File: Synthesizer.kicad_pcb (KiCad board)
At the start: 6 copper layers, 167 parts, among them J1 USB_A, J2 AudioJack3, J3 USB_B_Micro, J4 FPGA_debug, J5 MCU_debug, J6 67997-410HLF, SW1 SW_Push, SW10 SW_Push, SW11 SW_Push, SW12 SW_Push, SW13 SW_Push, SW14 SW_Push, SW15 SW_Push, SW16 SW_Push, SW2 SW_Push, SW3 SW_Push, SW4 SW_Push, SW5 SW_Push, SW6 SW_Push, SW7 SW_Push, SW8 SW_Push, SW9 SW_Push, U1 TPD3S014, U2 S25FL127S, U3 XC7A100T-FTG256, U4 Oscillator, U5 TPS54325, U6 TPS54294, U7 EFM32GG11B4xx, U8 PCM5102, Y1 48Mhz

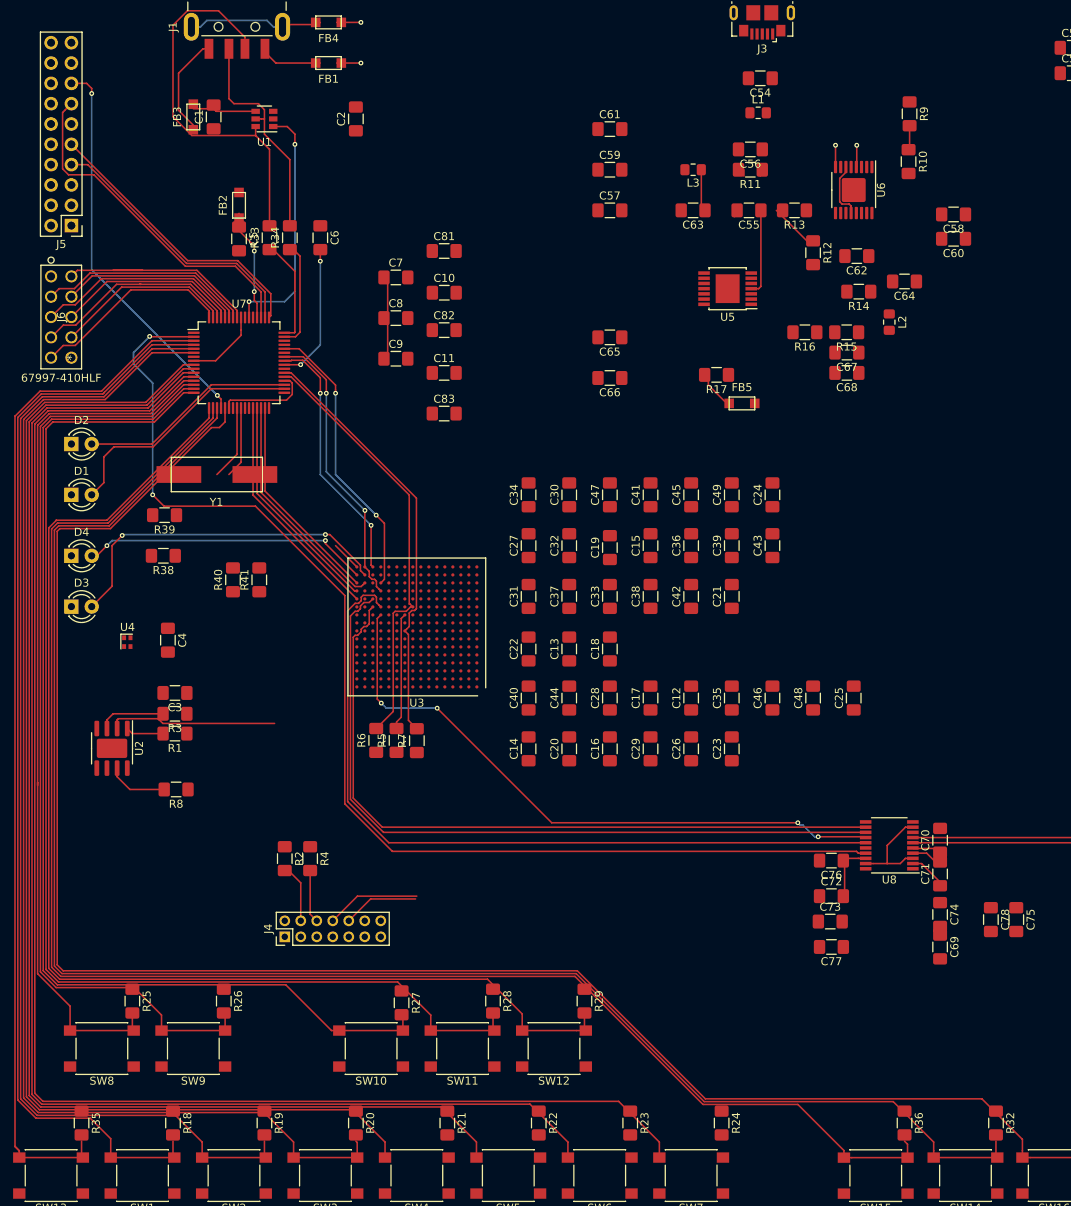
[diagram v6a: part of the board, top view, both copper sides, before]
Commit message: Added in the potentiometers, fixed some faulty pins on the artix, rewired some pins on the MCU so they didn't interfere with the crystal.
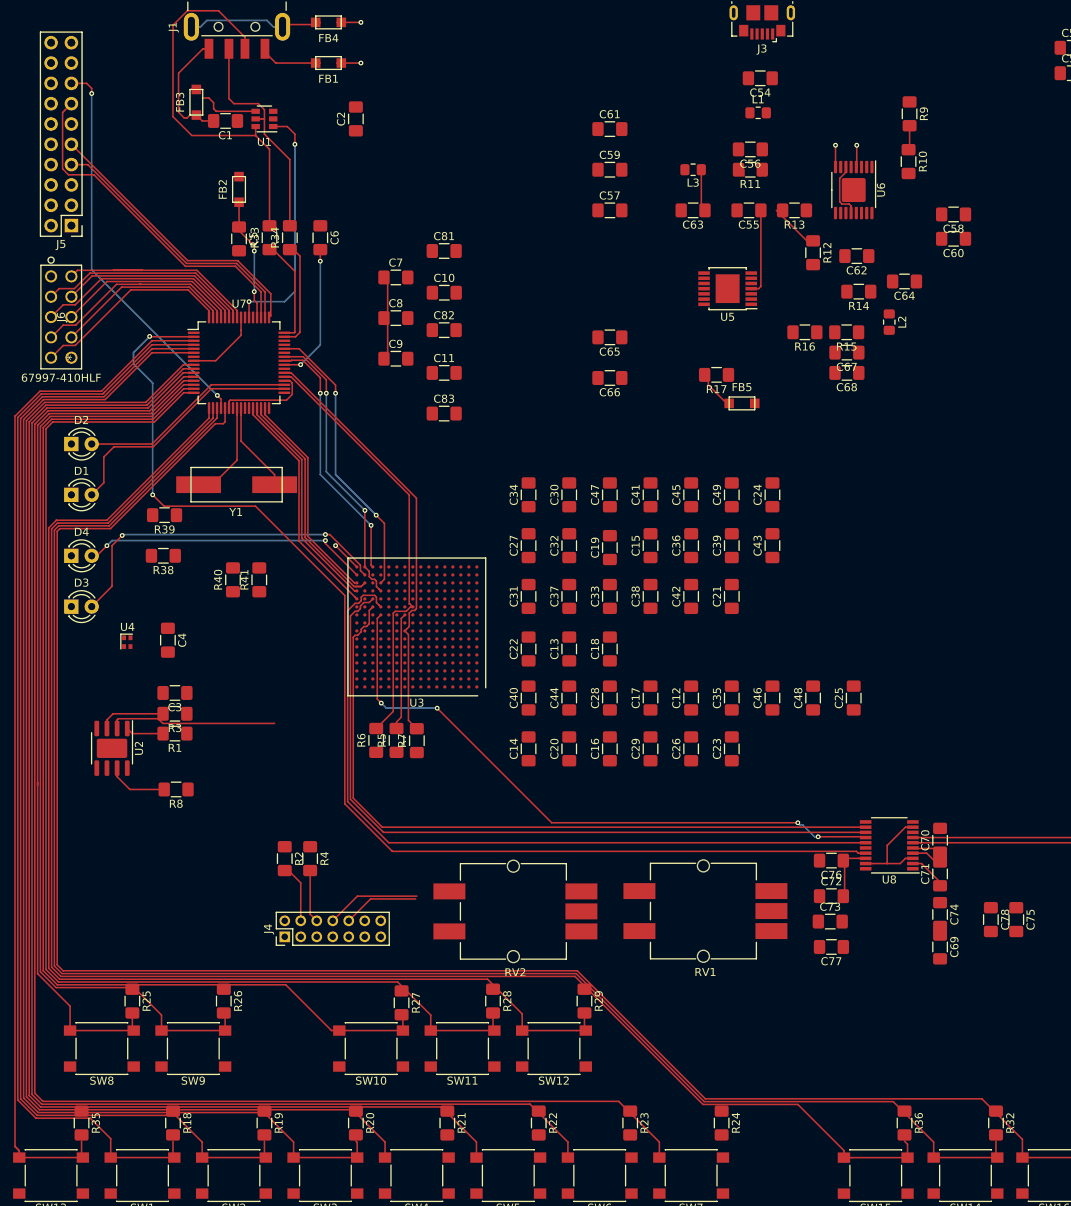
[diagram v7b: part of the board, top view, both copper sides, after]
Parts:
- added RV1: R_POT, Potentiometer_SMD:Potentiometer_Bourns_PRS11S_Vertical, F.Cu at (99.6, 125.7)
- added RV2: R_POT, Potentiometer_SMD:Potentiometer_Bourns_PRS11S_Vertical, F.Cu at (75.8, 125.7)
- moved Y1 2.77 mm to (41.0, 72.4)
- moved FB2 1.98 mm to (41.3, 35.5)
- moved FB3 1.88 mm to (35.9, 24.6)
- moved C1 1.57 mm to (39.6, 26.9), turned to 180 degrees
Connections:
- U7 pad 36: GND -> Net-(U7-Pad36)
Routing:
- net Net-(FB3-Pad1): track 0.00 -> 7.78 mm
- net Net-(C1-Pad2): track 20.2 -> 15.1 mm
- net Net-(U7-Pad24): track 9.35 -> 12.6 mm
- net Net-(U7-Pad25): track 8.94 -> 11.3 mm
- net /Artix7/SPI_CLK: track 28.6 -> 29.4 mm
- net Net-(C5-Pad1): track 14.3 -> 14.9 mm
- net GND: vias 6 -> 7
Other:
- board text added: "5V might need thicker trace"

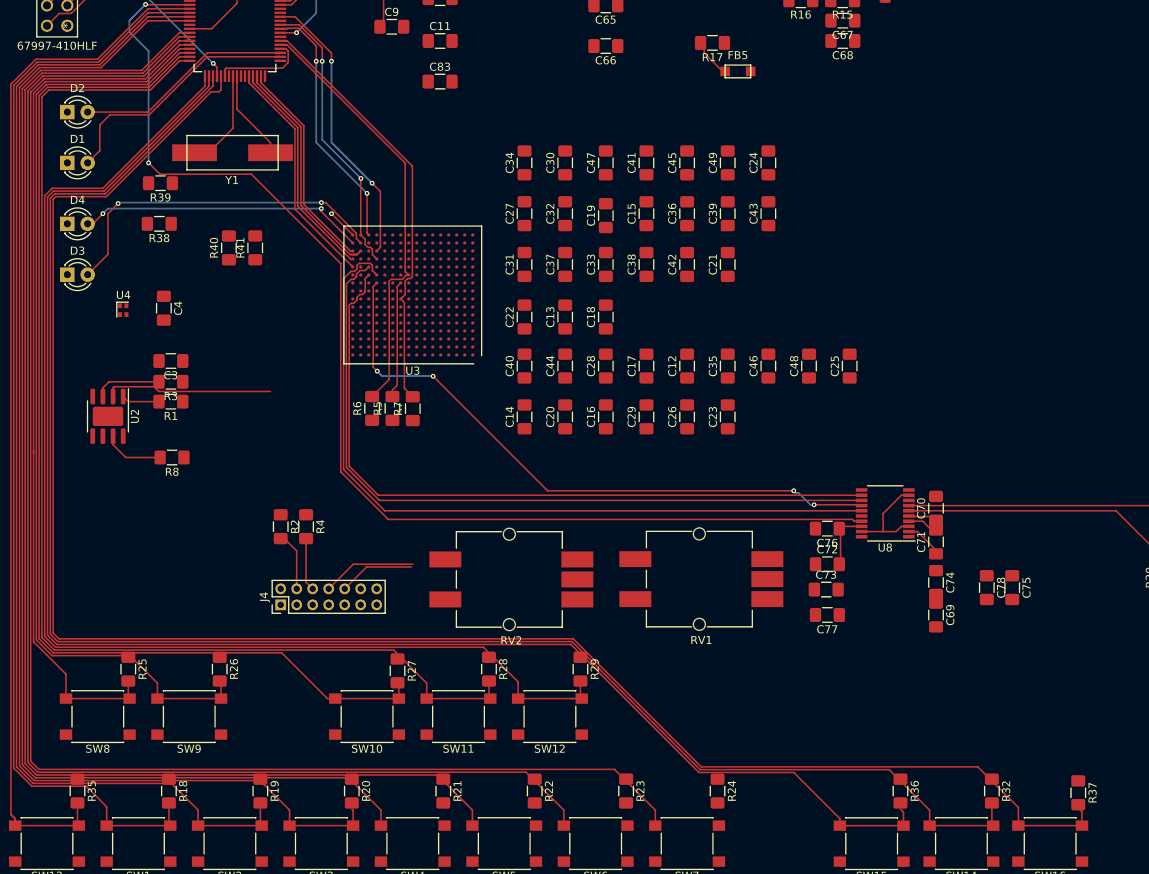
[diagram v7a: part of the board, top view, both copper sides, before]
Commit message: Wired up the potentiometers.
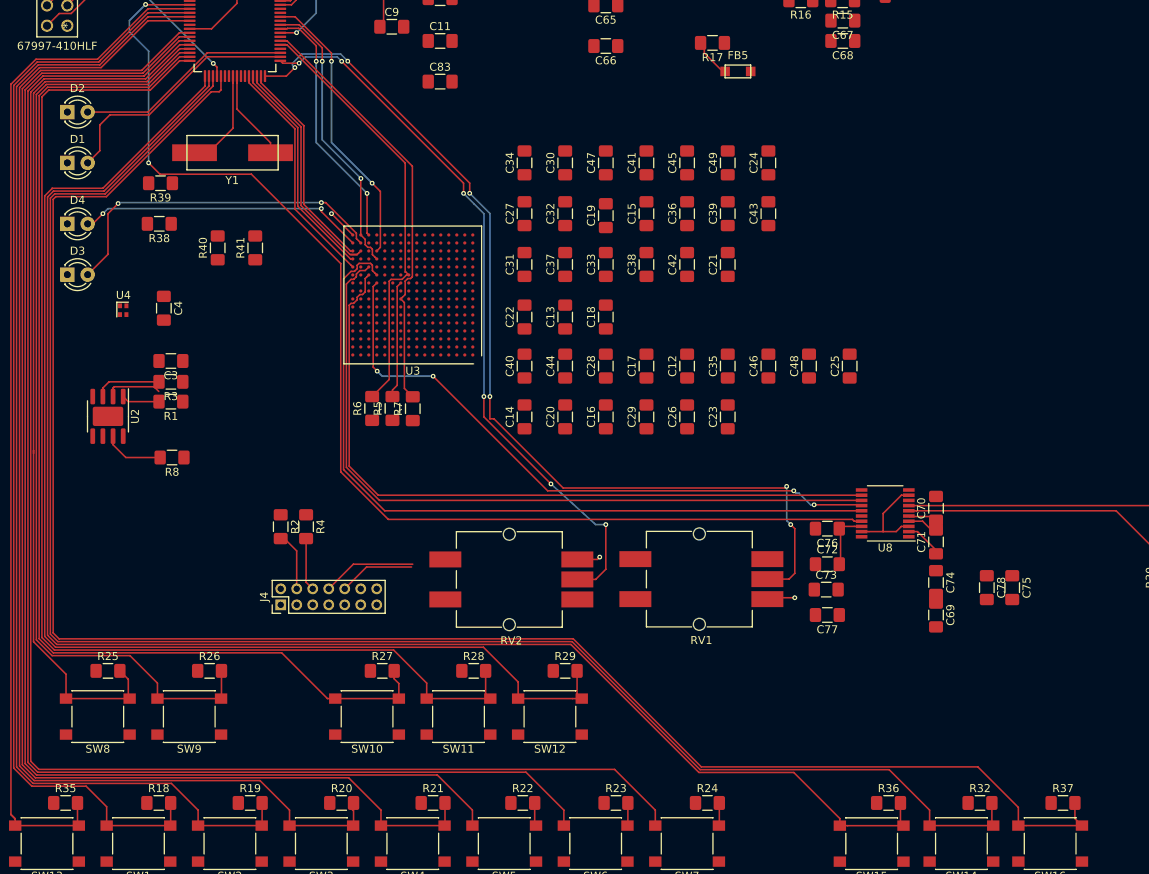
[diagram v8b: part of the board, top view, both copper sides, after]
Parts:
- moved R25 2.55 mm to (25.4, 137.2), turned to 0 degrees
- moved R37 2.29 mm to (144.8, 153.7), turned to 0 degrees
- moved R35 2.10 mm to (20.1, 153.7), turned to 0 degrees
- moved R22 2.10 mm to (77.3, 153.7), turned to 0 degrees
- moved R36 2.10 mm to (123.0, 153.7), turned to 0 degrees
- moved R32 2.10 mm to (134.4, 153.7), turned to 0 degrees
- moved R18 1.96 mm to (31.8, 153.7), turned to 0 degrees
- moved R19 1.96 mm to (43.2, 153.7), turned to 0 degrees
- moved R20 1.96 mm to (54.6, 153.7), turned to 0 degrees
- moved R21 1.96 mm to (66.0, 153.7), turned to 0 degrees
- moved R23 1.96 mm to (88.9, 153.7), turned to 0 degrees
- moved R24 1.96 mm to (100.3, 153.7), turned to 0 degrees
- moved R28 1.92 mm to (71.1, 137.2), turned to 0 degrees
- moved R29 1.92 mm to (82.5, 137.2), turned to 0 degrees
- moved R27 1.91 mm to (59.7, 137.2), turned to 0 degrees
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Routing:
- net Net-(RV1-Pad2): track 0.00 -> 120.4 mm, vias 0 -> 6
- net Net-(RV2-Pad2): track 0.00 -> 91.5 mm, vias 0 -> 6
- net Net-(U2-Pad2): track 21.1 -> 7.10 mm
- net GND: track 55.5 -> 43.9 mm
- net /Button4: track 157.4 -> 168.3 mm
- net +3V3: track 0.00 -> 6.42 mm, vias 0 -> 2
- net /Button5: track 167.8 -> 170.7 mm
- net /Button6: track 178.1 -> 181.0 mm
- net /Button7: track 188.5 -> 191.3 mm
- net /Button8: track 109.7 -> 111.6 mm
- net /Button12: track 155.7 -> 157.6 mm
- net /Button11: track 150.5 -> 152.2 mm
- net /Button10: track 138.9 -> 140.5 mm
- net /Button9: track 118.9 -> 120.2 mm
- net /Button3: track 157.6 -> 158.5 mm
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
